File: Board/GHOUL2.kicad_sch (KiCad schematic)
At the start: 15 parts, among them Q1 IRF540N, Q2 IRF540N, U1 Teensy3.5_All_Pins, U10 GHOULIMU, U2 LM7805_TO220, U3 BMP280, U4 Feedback_Serv, U5 LM1084-ADJ, U6 NichromeConnector, U7 Ultimate_GPS_Breakout_v3, U8 Xbee, U9 NichromeConnector

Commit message: did a layout, needs some more work but at least it exists now
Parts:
- added J1: Conn_01x02, Connector_AMASS:AMASS_XT30PW-M_1x02_P2.50mm_Horizontal, symbol Connector_Generic:Conn_01x02
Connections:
- net +9V: now also J1.2 (Pin_2); no longer C1.1
- net 5v pwr: now also C1.1
- net GND: now also J1.1 (Pin_1)
- net at U5.2 (VO): now also R1.3; no longer R1.2
- net at U1.9 (7_RX3_MOSI0_SCL0), U10.6 (SCL), U3.4 (SCK): no longer U1.76 (47_RX6_SCL0)
- net at U1.10 (8_TX3_MISO0_SDA0), U10.7 (SDA), U3.5 (SDO): no longer U1.77 (48_TX6_SDA0)
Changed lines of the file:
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@@
   (junction (at 96.52 53.34) (diameter 0) (color 0 0 0 0)
   )
-  (junction (at 231.14 63.5) (diameter 0) (color 0 0 0 0)
-  )
   (junction (at 59.69 78.74) (diameter 0) (color 0 0 0 0)
   )
@@
   (junction (at 110.49 57.15) (diameter 0) (color 0 0 0 0)
   )
-  (junction (at 231.14 66.04) (diameter 0) (color 0 0 0 0)
-  )
   (junction (at 59.69 71.12) (diameter 0) (color 0 0 0 0)
   )
@@
     (stroke (width 0) (type default) (color 0 0 0 0))
   )
+  (wire (pts (xy 97.79 53.34) (xy 97.79 49.53))
+    (stroke (width 0) (type default) (color 0 0 0 0))
+  )
   (wire (pts (xy 247.65 77.47) (xy 198.12 77.47))
     (stroke (width 0) (type default) (color 0 0 0 0))
@@
   )
   (wire (pts (xy 250.19 113.03) (xy 238.76 113.03))
+    (stroke (width 0) (type default) (color 0 0 0 0))
+  )
+  (wire (pts (xy 97.79 49.53) (xy 114.3 49.53))
     (stroke (width 0) (type default) (color 0 0 0 0))
   )
@@
     (stroke (width 0) (type default) (color 0 0 0 0))
   )
-  (wire (pts (xy 231.14 66.04) (xy 236.22 66.04))
+  (wire (pts (xy 232.41 64.77) (xy 236.22 66.04))
     (stroke (width 0) (type default) (color 0 0 0 0))
   )
@@
     (stroke (width 0) (type default) (color 0 0 0 0))
   )
+  (wire (pts (xy 114.3 49.53) (xy 114.3 40.64))
+    (stroke (width 0) (type default) (color 0 0 0 0))
+  )
   (wire (pts (xy 96.52 40.64) (xy 99.06 40.64))
     (stroke (width 0) (type default) (color 0 0 0 0))
@@
     (stroke (width 0) (type default) (color 0 0 0 0))
   )
-  (wire (pts (xy 172.72 63.5) (xy 231.14 63.5))
+  (wire (pts (xy 172.72 63.5) (xy 231.14 62.23))
     (stroke (width 0) (type default) (color 0 0 0 0))
   )
@@
     (stroke (width 0) (type default) (color 0 19 255 1))
   )
-  (wire (pts (xy 96.52 53.34) (xy 97.79 53.34))
-    (stroke (width 0) (type default) (color 0 0 0 0))
-  )
   (wire (pts (xy 59.69 78.74) (xy 59.69 71.12))
     (stroke (width 0) (type default) (color 0 0 0 0))
@@
     (stroke (width 0) (type default) (color 0 0 0 0))
   )
-  (wire (pts (xy 217.17 66.04) (xy 231.14 66.04))
+  (wire (pts (xy 217.17 66.04) (xy 232.41 64.77))
     (stroke (width 0) (type default) (color 0 0 0 0))
   )
@@
     (stroke (width 0) (type default) (color 0 0 0 0))
   )
-  (wire (pts (xy 231.14 63.5) (xy 238.76 63.5))
+  (wire (pts (xy 231.14 62.23) (xy 238.76 63.5))
     (stroke (width 0) (type default) (color 0 0 0 0))
   )
@@
     )
   )
+  (global_label "Vin" (shape input) (at 96.52 40.64 180) (fields_autoplaced)
+    (effects (font (size 1.27 1.27)) (justify right))
+    (property "Intersheet References" "${INTERSHEET_REFS}" (id 0) (at 91.2645 40.5606 0)
+      (effects (font (size 1.27 1.27)) (justify right) hide)
+    )
+  )
   (global_label "5v pwr" (shape input) (at 114.3 40.64 0) (fields_autoplaced)
     (effects (font (size 1.27 1.27)) (justify left))
@@
     (property "Intersheet References" "${INTERSHEET_REFS}" (id 0) (at 103.1664 107.8706 0)
       (effects (font (size 1.27 1.27)) (justify left) hide)
+    )
+  )
+  (global_label "Vin" (shape input) (at 262.89 34.29 180) (fields_autoplaced)
+    (effects (font (size 1.27 1.27)) (justify right))
+    (property "Intersheet References" "${INTERSHEET_REFS}" (id 0) (at 257.6345 34.2106 0)
+      (effects (font (size 1.27 1.27)) (justify right) hide)
     )
   )
@@
   (symbol (lib_id "Device:R") (at 55.88 71.12 270) (unit 1)
     (in_bom yes) (on_board yes) (fields_autoplaced)
-    (property "Reference" "R1" (id 0) (at 55.88 64.77 90))
-    (property "Value" "03" (id 1) (at 55.88 67.31 90))
-    (property "Footprint" "Package_TO_SOT_SMD:TO-263-2" (id 2) (at 55.88 69.342 90)
+    (property "Reference" "R1" (id 0) (at 62.23 71.12 90))
+    (property "Value" "03" (id 1) (at 59.69 71.12 90))
+    (property "Footprint" "Package_TO_SOT_SMD:TO-263-2" (id 2) (at 57.658 71.12 90)
       (effects (font (size 1.27 1.27)) hide)
     )
@@
     )
     (pin "1")
-    (pin "2")
+    (pin "3")
   )
   (symbol (lib_id "power:GND") (at 172.72 40.64 270) (unit 1)
@@
     (pin "3")
     (pin "4")
+  )
+  (symbol (lib_id "power:GND") (at 262.89 31.75 270) (unit 1)
+    (in_bom yes) (on_board yes)
+    (property "Reference" "#PWR0111" (id 0) (at 256.54 31.75 0)
+      (effects (font (size 1.27 1.27)) hide)
+    )
+    (property "Value" "GND" (id 1) (at 255.27 31.75 90)
+      (effects (font (size 1.27 1.27)) (justify left))
+    )
+    (property "Footprint" "" (id 2) (at 262.89 31.75 0)
+      (effects (font (size 1.27 1.27)) hide)
+    )
+    (property "Datasheet" "" (id 3) (at 262.89 31.75 0)
+      (effects (font (size 1.27 1.27)) hide)
+    )
+    (pin "1")
   )
   (symbol (lib_id "GHOUL:NichromeConnector") (at 69.85 68.58 0) (unit 1)
@@
     )
     (pin "1")
+  )
+  (symbol (lib_id "Connector_Generic:Conn_01x02") (at 267.97 31.75 0) (unit 1)
+    (in_bom yes) (on_board yes) (fields_autoplaced)
+    (property "Reference" "J1" (id 0) (at 270.51 31.7499 0)
+      (effects (font (size 1.27 1.27)) (justify left))
+    )
+    (property "Value" "Conn_01x02" (id 1) (at 270.51 34.2899 0)
+      (effects (font (size 1.27 1.27)) (justify left))
+    )
+    (property "Footprint" "Connector_AMASS:AMASS_XT30PW-M_1x02_P2.50mm_Horizontal" (id 2) (at 267.97 31.75 0)
+      (effects (font (size 1.27 1.27)) hide)
+    )
+    (property "Datasheet" "~" (id 3) (at 267.97 31.75 0)
+      (effects (font (size 1.27 1.27)) hide)
+    )
+    (pin "1")
+    (pin "2")
   )
   (symbol (lib_id "power:GND") (at 149.86 99.06 90) (unit 1)
@@
       (reference "#PWR0110") (unit 1) (value "GND") (footprint "")
     )
+    (path "/707fed9e-5b9e-40a5-a3f5-afb695484dbb"
+      (reference "#PWR0111") (unit 1) (value "GND") (footprint "")
+    )
     (path "/e100fb02-ae0f-4575-a8f0-e7fb3c16a01e"
       (reference "BT1") (unit 1) (value "Battery_Cell") (footprint "Battery:BatteryHolder_Keystone_3000_1x12mm")
@@
       (reference "C1") (unit 1) (value "C 10 nano-farad") (footprint "GHOULFootPrints:GhoulResistor")
     )
+    (path "/9902bfe6-8d4f-44df-947a-5e52f92861a4"
+      (reference "J1") (unit 1) (value "Conn_01x02") (footprint "Connector_AMASS:AMASS_XT30PW-M_1x02_P2.50mm_Horizontal")
+    )
     (path "/2fd90422-ba41-4885-811c-3484a05fc047"

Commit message: fixed goofy-ah xbee footprint (sch update)
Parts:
- U6, U9: footprint Connector_PinSocket_2.54mm:PinSocket_1x02_P2.54mm_Vertical -> Connector_JST:JST_EH_B2B-EH-A_1x02_P2.50mm_Vertical
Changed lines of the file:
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@@
       (effects (font (size 1.27 1.27)) (justify left))
     )
-    (property "Footprint" "Connector_PinSocket_2.54mm:PinSocket_1x02_P2.54mm_Vertical" (id 2) (at 69.85 86.36 0)
+    (property "Footprint" "Connector_JST:JST_EH_B2B-EH-A_1x02_P2.50mm_Vertical" (id 2) (at 69.85 86.36 0)
       (effects (font (size 1.27 1.27)) hide)
     )
@@
       (effects (font (size 1.27 1.27)) (justify left))
     )
-    (property "Footprint" "Connector_PinSocket_2.54mm:PinSocket_1x02_P2.54mm_Vertical" (id 2) (at 69.85 68.58 0)
+    (property "Footprint" "Connector_JST:JST_EH_B2B-EH-A_1x02_P2.50mm_Vertical" (id 2) (at 69.85 68.58 0)
       (effects (font (size 1.27 1.27)) hide)
     )
@@
     )
     (path "/734a620d-4445-45de-a54d-e8d8da70fce4"
-      (reference "U6") (unit 1) (value "NichromeConnector") (footprint "Connector_PinSocket_2.54mm:PinSocket_1x02_P2.54mm_Vertical")
+      (reference "U6") (unit 1) (value "NichromeConnector") (footprint "Connector_JST:JST_EH_B2B-EH-A_1x02_P2.50mm_Vertical")
     )
     (path "/844dbbcd-0ee2-4f2b-9780-c9edf1ec87d7"
@@
     )
     (path "/15b37397-972a-4870-a143-25e9781a6e82"
-      (reference "U9") (unit 1) (value "NichromeConnector") (footprint "Connector_PinSocket_2.54mm:PinSocket_1x02_P2.54mm_Vertical")
+      (reference "U9") (unit 1) (value "NichromeConnector") (footprint "Connector_JST:JST_EH_B2B-EH-A_1x02_P2.50mm_Vertical")
     )
     (path "/ee1da804-b043-48ee-a3cd-e6aabe5242f6"

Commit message: lots of improvements
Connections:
- net Nic1: now also U1.33 (36_A17_PWM); no longer U1.8 (6_PWM)
- net Nic2: now also U1.32 (35_A16_PWM); no longer U1.4 (2_PWM)
- net at U1.22 (30_PWM_CAN0RX_Touch): no longer U4.1 (PWM)
- net at U1.2 (0_RX1_MOSI1_Touch): no longer U8.3 (Dout)
- net at U1.3 (1_TX1_MISO1_Touch): no longer U8.4 (Din)
- net SCL: now reaches U1.9 (7_RX3_MOSI0_SCL0), U10.6 (SCL), U3.4 (SCK)
- net SDA: now reaches U1.10 (8_TX3_MISO0_SDA0), U10.7 (SDA), U3.5 (SDO)
- net 3v3 pwr: now reaches U1.15 (3.3V)
- net 3v3 pwr: now also U10.1 (VIN)
- net Xbee DIn: now reaches U1.18 (26_TX1_SCL2)
- net Xbee DIn: now also U8.4 (Din)
- net Xbee DOut: now reaches U1.19 (27_RX1_SCK0)
- net Xbee DOut: now also U8.3 (Dout)
- net at U1.51 (3.3V): no longer U10.1 (VIN)
- new net Servo PWM: U1.4 (2_PWM), U4.1 (PWM)
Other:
- moved on the sheet: U3, U4

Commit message: for real this time... ?
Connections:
- net GND: now also R1.2
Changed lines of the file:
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@@
+    (stroke (width 0) (type default) (color 0 0 0 0))
+  )
+  (wire (pts (xy 55.88 60.96) (xy 55.88 67.31))
     (stroke (width 0) (type default) (color 0 0 0 0))
   )
@@
   (symbol (lib_id "Device:R") (at 55.88 71.12 270) (unit 1)
     (in_bom yes) (on_board yes) (fields_autoplaced)
-    (property "Reference" "R1" (id 0) (at 62.23 71.12 90))
-    (property "Value" "03" (id 1) (at 59.69 71.12 90))
-    (property "Footprint" "Package_TO_SOT_SMD:TO-263-2" (id 2) (at 57.658 71.12 90)
+    (property "Reference" "R1" (id 0) (at 55.88 64.77 90))
+    (property "Value" "03" (id 1) (at 55.88 67.31 90))
+    (property "Footprint" "Package_TO_SOT_SMD:TO-263-2" (id 2) (at 55.88 69.342 90)
       (effects (font (size 1.27 1.27)) hide)
     )
@@
     )
     (pin "1")
+    (pin "2")
     (pin "3")
   )
@@
     )
     (property "Datasheet" "" (id 3) (at 148.59 49.53 0)
+      (effects (font (size 1.27 1.27)) hide)
+    )
+    (pin "1")
+  )
+  (symbol (lib_id "power:GND") (at 55.88 60.96 180) (unit 1)
+    (in_bom yes) (on_board yes)
+    (property "Reference" "#PWR0112" (id 0) (at 55.88 54.61 0)
+      (effects (font (size 1.27 1.27)) hide)
+    )
+    (property "Value" "GND" (id 1) (at 55.88 53.34 90)
+      (effects (font (size 1.27 1.27)) (justify left))
+    )
+    (property "Footprint" "" (id 2) (at 55.88 60.96 0)
+      (effects (font (size 1.27 1.27)) hide)
+    )
+    (property "Datasheet" "" (id 3) (at 55.88 60.96 0)
       (effects (font (size 1.27 1.27)) hide)
     )
@@
       (reference "#PWR0111") (unit 1) (value "GND") (footprint "")
     )
+    (path "/c766f8cf-c139-4fb1-afd5-9c039f651864"
+      (reference "#PWR0112") (unit 1) (value "GND") (footprint "")
+    )
     (path "/e100fb02-ae0f-4575-a8f0-e7fb3c16a01e"

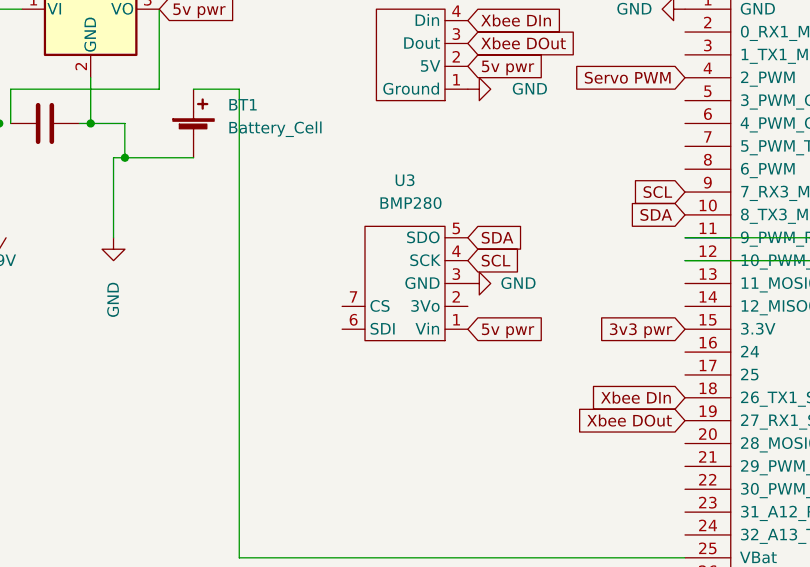
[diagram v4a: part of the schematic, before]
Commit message: fixed schematic and brd bmp280 miswiring
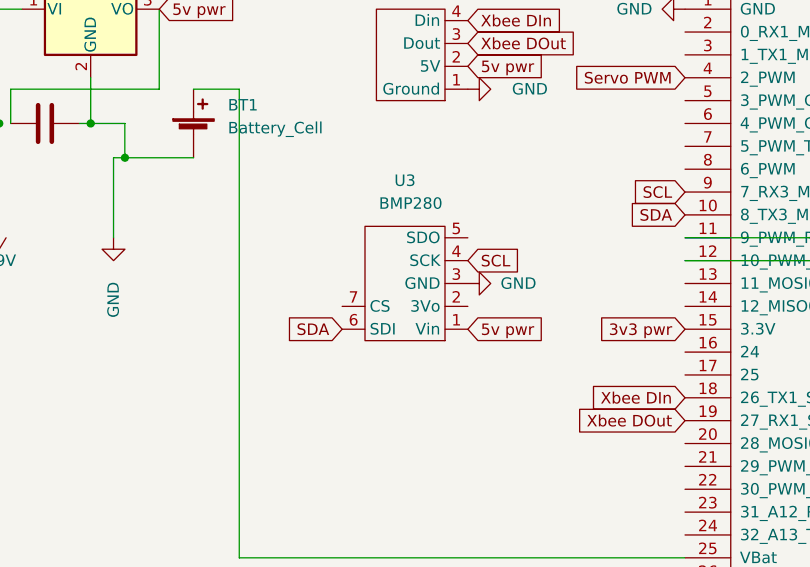
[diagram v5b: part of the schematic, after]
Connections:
- net SDA: now also U3.6 (SDI); no longer U3.5 (SDO)
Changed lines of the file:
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@@
-    )
-  )
-  (global_label "SDA" (shape input) (at 148.59 66.04 0) (fields_autoplaced)
-    (effects (font (size 1.27 1.27)) (justify left))
-    (property "Intersheet References" "${INTERSHEET_REFS}" (id 0) (at 154.5712 65.9606 0)
-      (effects (font (size 1.27 1.27)) (justify left) hide)
     )
   )
@@
       (effects (font (size 1.27 1.27)) (justify right) hide)
     )
+  )
+  (global_label "SDA" (shape input) (at 134.62 76.2 180) (fields_autoplaced)
+    (effects (font (size 1.27 1.27)) (justify right))
+    (property "Intersheet References" "${INTERSHEET_REFS}" (id 0) (at 128.6388 76.2794 0)
+      (effects (font (size 1.27 1.27)) (justify right) hide)
+    )

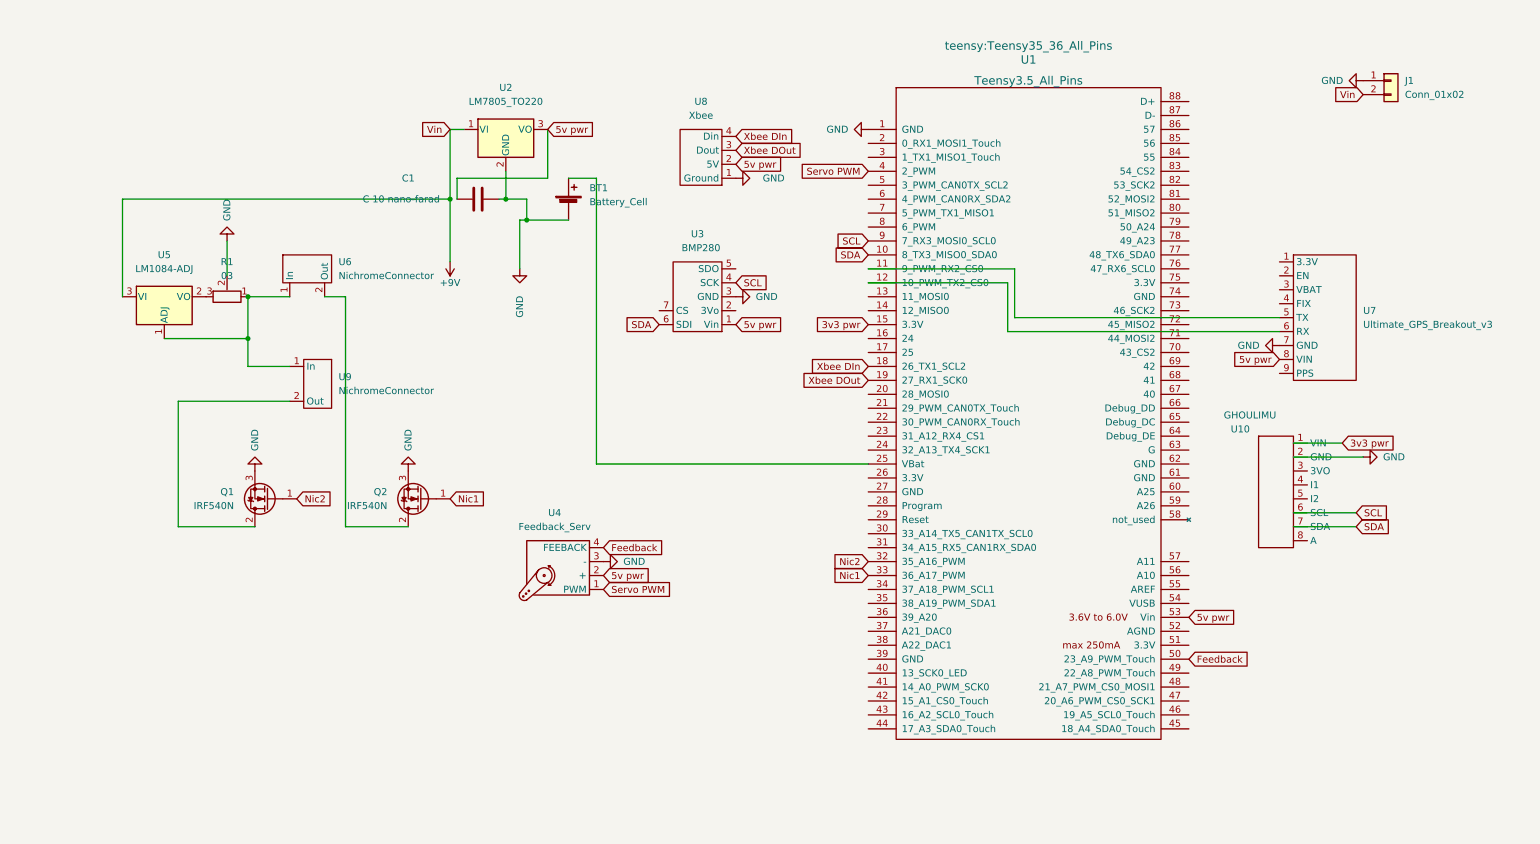
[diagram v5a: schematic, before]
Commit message: Schematic clarity improvements
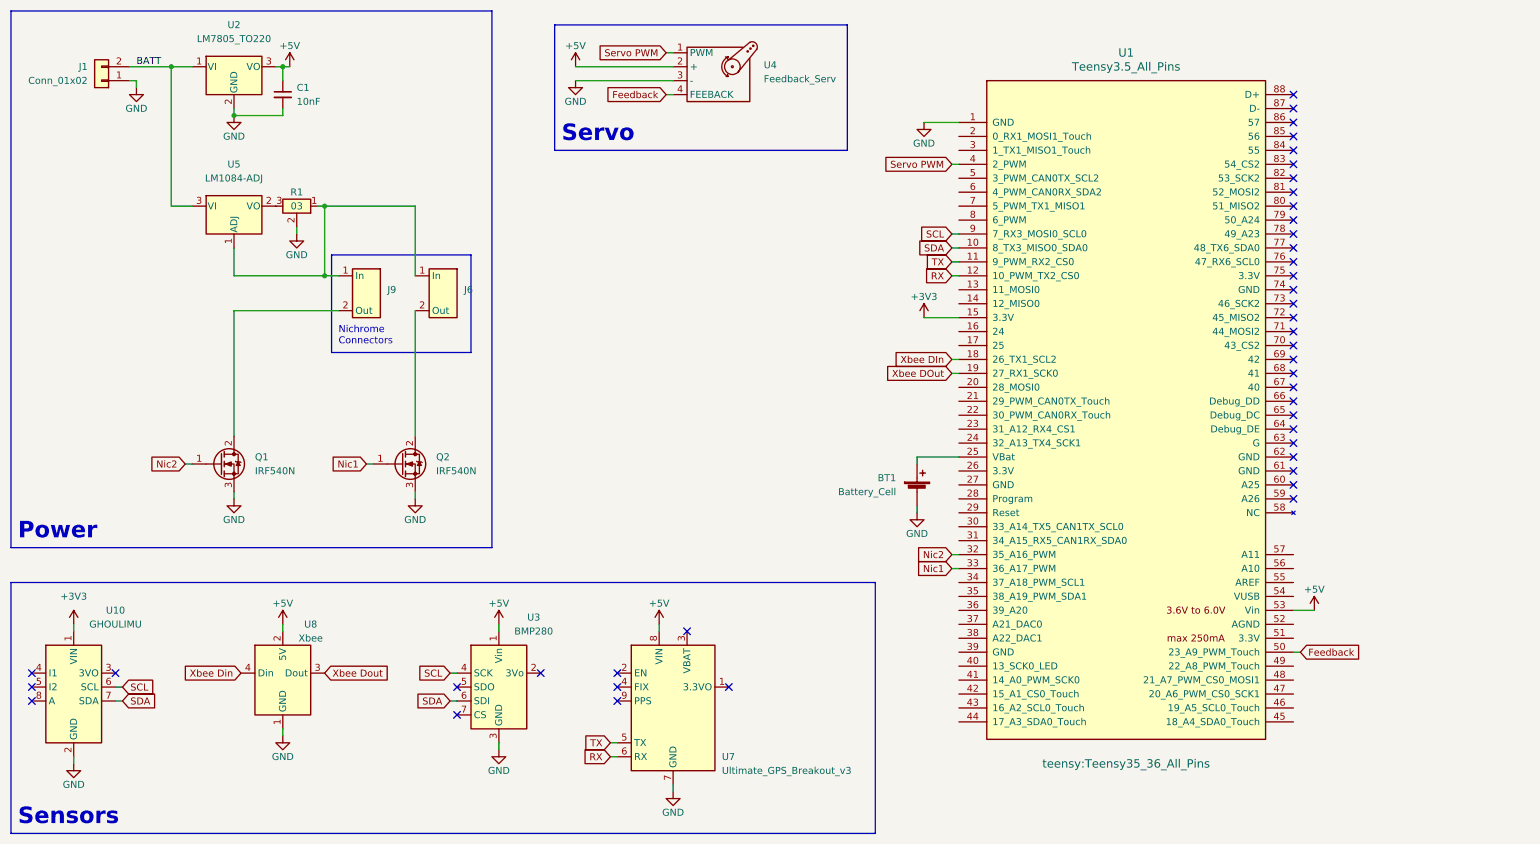
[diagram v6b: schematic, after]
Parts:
- removed C1: C 10 nano-farad, GHOULFootPrints:GhoulResistor, symbol Device:C
- added C1: 10nF, symbol Device:C_Small
- J6: renamed from U6; value NichromeConnector -> Nichrome Connector
- J9: renamed from U9; value NichromeConnector -> Nichrome Connector
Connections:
- net GND: now also C1.2
- net Xbee DIn: no longer U8.4 (Din)
- net Xbee DOut: no longer U8.3 (Dout)
- net TX: now reaches U1.11 (9_PWM_RX2_CS0), U7.5 (TX)
- net RX: now reaches U1.12 (10_PWM_TX2_CS0), U7.6 (RX)
- net +9V renamed BATT
- net 3v3 pwr renamed +3V3
- net 5v pwr renamed +5V
- net +5V: now also C1.1
- new net Xbee Din: U8.4 (Din)
- new net Xbee Dout: U8.3 (Dout)
- no-connect marks 0 -> 42
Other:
- note added: "Nichrome Connectors"
- note added: "Power"
- note added: "Sensors"
- note added: "Servo"
- company: (none) -> JJ Kuznetsov
- title: (none) -> GHOUL Mainboard
- moved on the sheet: BT1, J1, Q1, Q2, U2, U4, U5
